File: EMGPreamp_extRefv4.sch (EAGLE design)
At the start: 33 parts

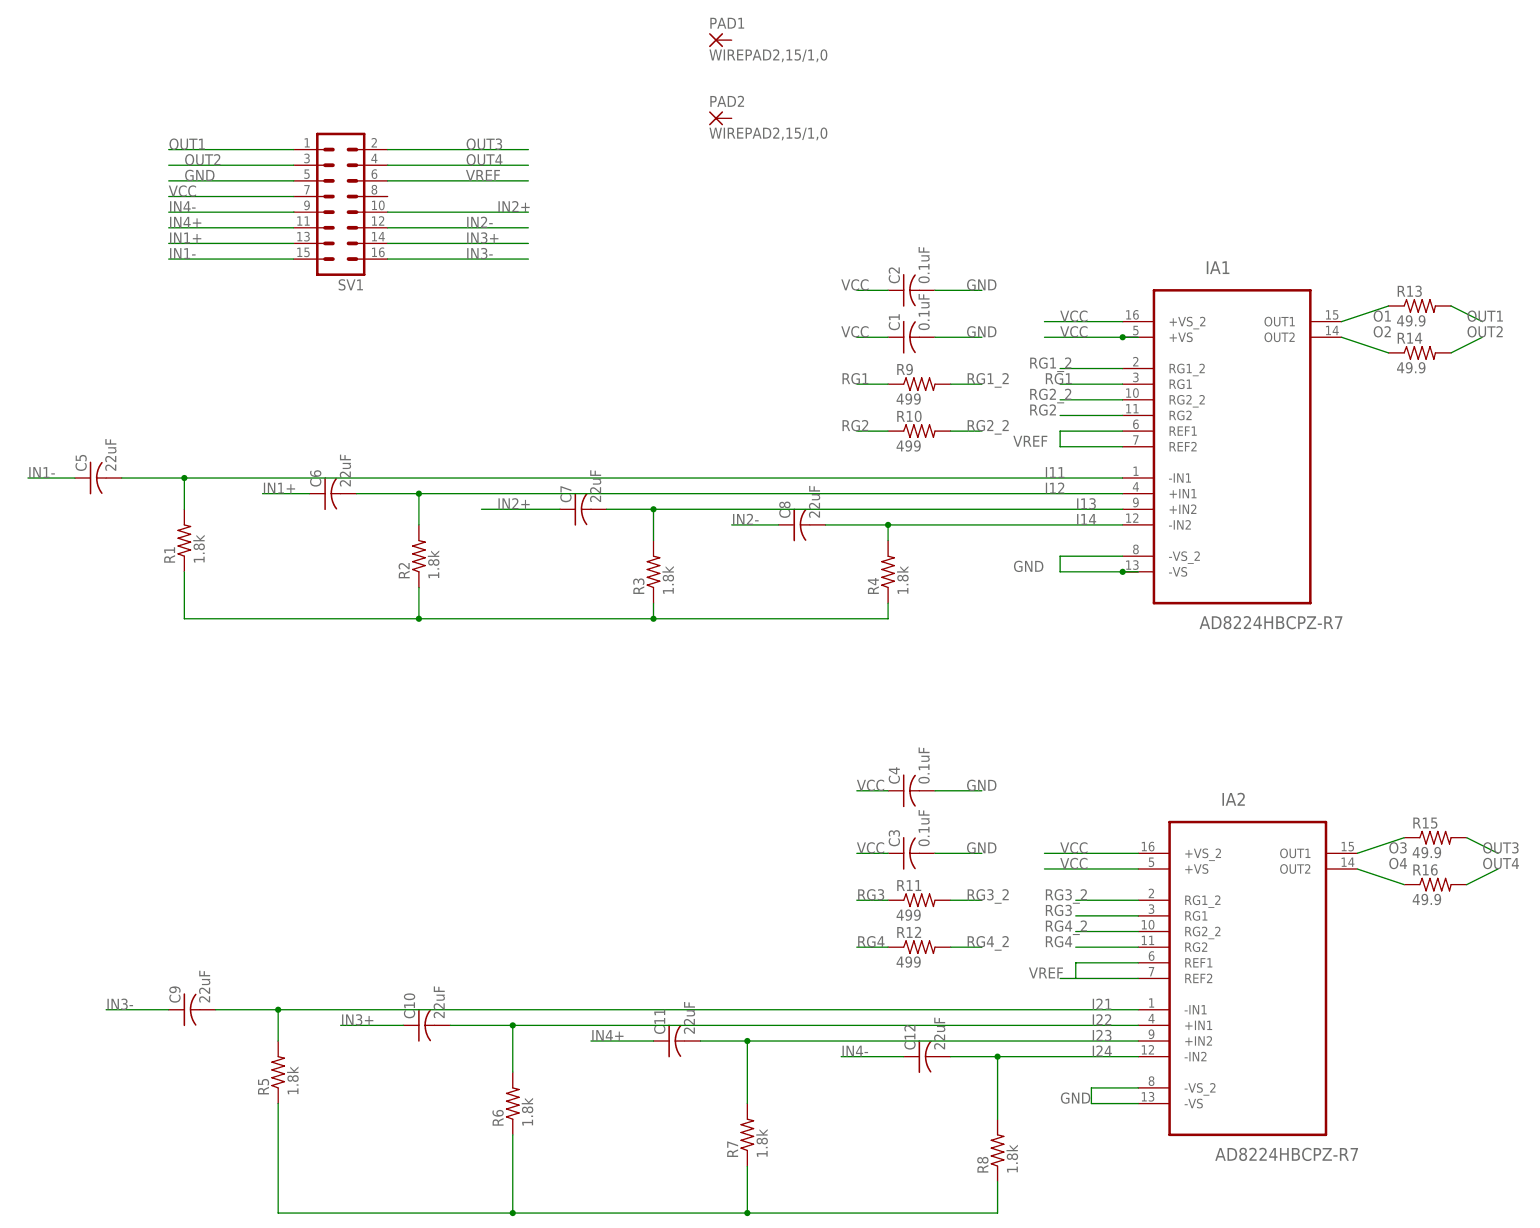
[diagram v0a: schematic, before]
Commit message: updated power board designs: v2 uses low current 2.5v reference, v3 uses 10v rail and 5v ref both with simple linear regulators. Added breakout board to go from DB37 to BNC
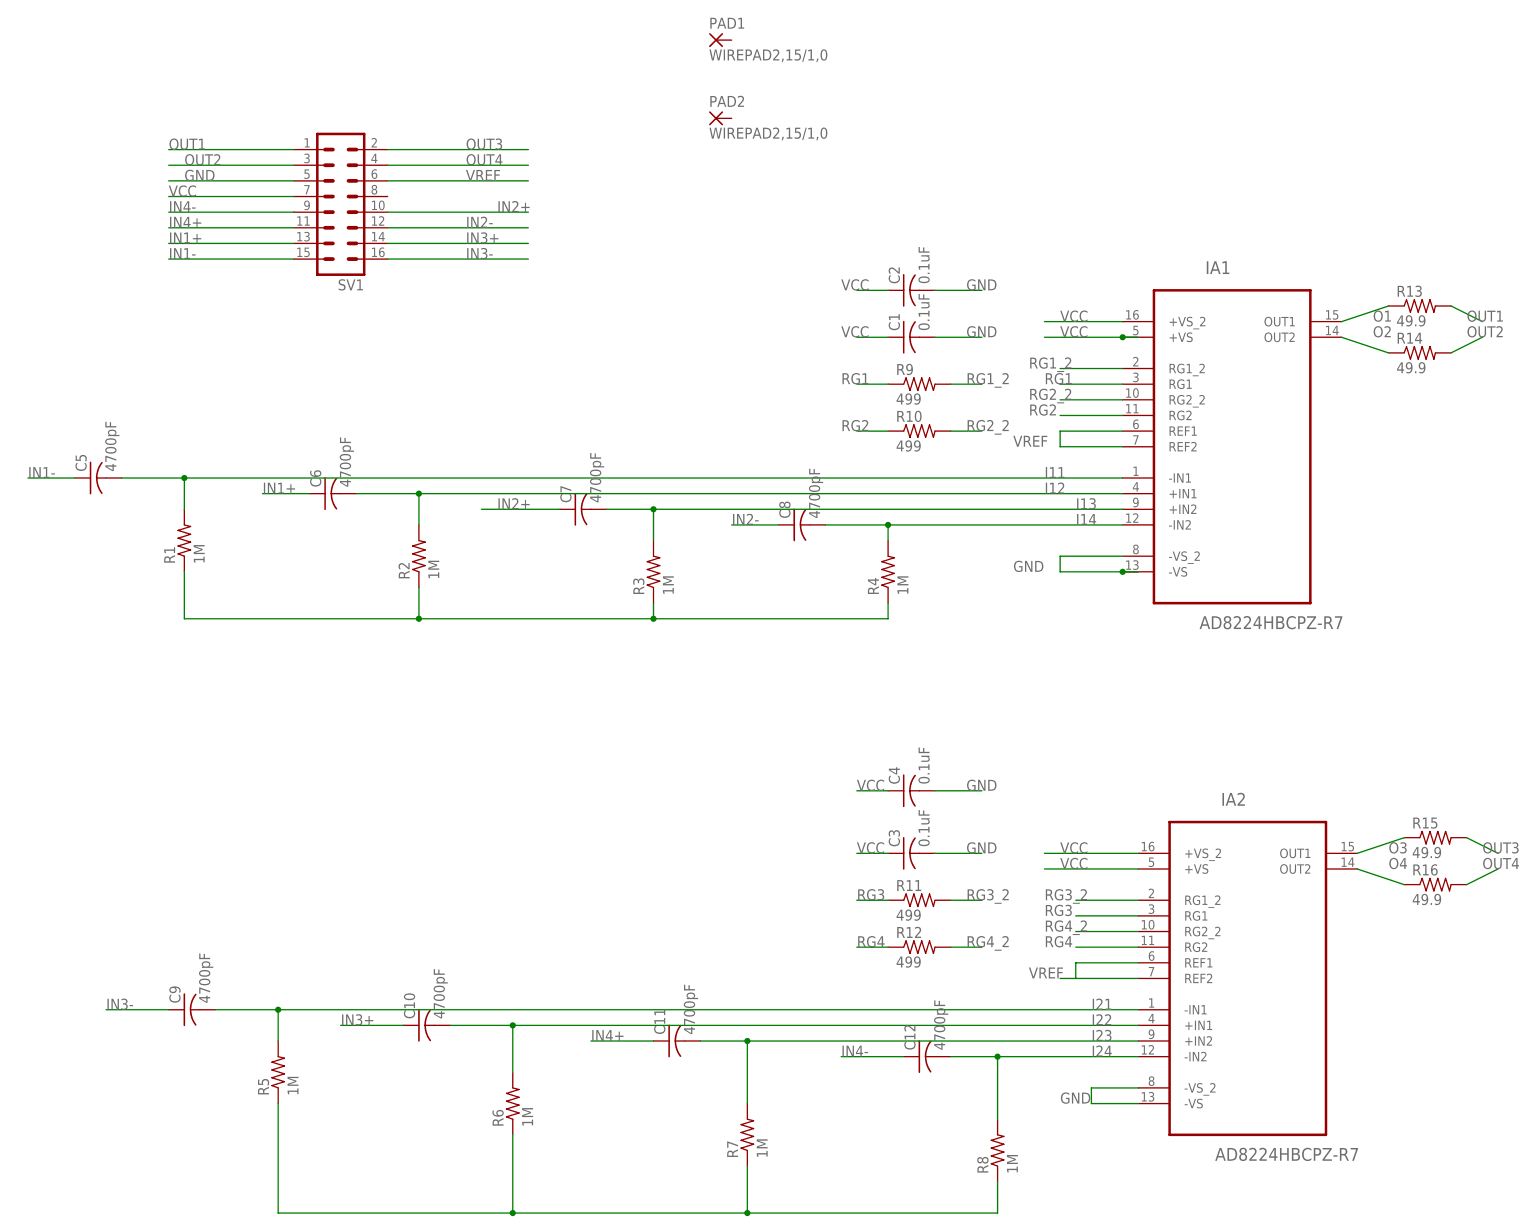
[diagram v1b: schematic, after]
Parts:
- C10, C11, C12, C5, C6, C7, C8, C9: value 22uF -> 4700pF
- R1, R2, R3, R4, R5, R6, R7, R8: value 1.8k -> 1M
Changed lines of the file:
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@@
 <part name="R11" library="rcl" deviceset="R-US_" device="R0805" value="499"/>
 <part name="R12" library="rcl" deviceset="R-US_" device="R0805" value="499"/>
-<part name="C5" library="rcl" deviceset="C-US" device="C0805" value="22uF"/>
-<part name="C6" library="rcl" deviceset="C-US" device="C0805" value="22uF"/>
-<part name="C7" library="rcl" deviceset="C-US" device="C0805" value="22uF"/>
-<part name="C8" library="rcl" deviceset="C-US" device="C0805" value="22uF"/>
-<part name="C9" library="rcl" deviceset="C-US" device="C0805" value="22uF"/>
-<part name="C10" library="rcl" deviceset="C-US" device="C0805" value="22uF"/>
-<part name="C11" library="rcl" deviceset="C-US" device="C0805" value="22uF"/>
-<part name="C12" library="rcl" deviceset="C-US" device="C0805" value="22uF"/>
+<part name="C5" library="rcl" deviceset="C-US" device="C0805" value="4700pF"/>
+<part name="C6" library="rcl" deviceset="C-US" device="C0805" value="4700pF"/>
+<part name="C7" library="rcl" deviceset="C-US" device="C0805" value="4700pF"/>
+<part name="C8" library="rcl" deviceset="C-US" device="C0805" value="4700pF"/>
+<part name="C9" library="rcl" deviceset="C-US" device="C0805" value="4700pF"/>
+<part name="C10" library="rcl" deviceset="C-US" device="C0805" value="4700pF"/>
+<part name="C11" library="rcl" deviceset="C-US" device="C0805" value="4700pF"/>
+<part name="C12" library="rcl" deviceset="C-US" device="C0805" value="4700pF"/>
 <part name="C1" library="rcl" deviceset="C-US" device="C0805" value="0.1uF"/>
 <part name="C2" library="rcl" deviceset="C-US" device="C0805" value="0.1uF"/>
@@
 <part name="PAD2" library="wirepad" deviceset="WIREPAD" device="2,15/1,0" value="WIREPAD2,15/1,0"/>
 <part name="SV1" library="con-lstb" deviceset="MA08-2W" device=""/>
-<part name="R1" library="resistor" deviceset="R-US_" device="R0805" value="1.8k"/>
-<part name="R2" library="resistor" deviceset="R-US_" device="R0805" value="1.8k"/>
-<part name="R3" library="resistor" deviceset="R-US_" device="R0805" value="1.8k"/>
-<part name="R4" library="resistor" deviceset="R-US_" device="R0805" value="1.8k"/>
-<part name="R5" library="resistor" deviceset="R-US_" device="R0805" value="1.8k"/>
-<part name="R6" library="resistor" deviceset="R-US_" device="R0805" value="1.8k"/>
-<part name="R7" library="resistor" deviceset="R-US_" device="R0805" value="1.8k"/>
-<part name="R8" library="resistor" deviceset="R-US_" device="R0805" value="1.8k"/>
+<part name="R1" library="resistor" deviceset="R-US_" device="R0805" value="1M"/>
+<part name="R2" library="resistor" deviceset="R-US_" device="R0805" value="1M"/>
+<part name="R3" library="resistor" deviceset="R-US_" device="R0805" value="1M"/>
+<part name="R4" library="resistor" deviceset="R-US_" device="R0805" value="1M"/>
+<part name="R5" library="resistor" deviceset="R-US_" device="R0805" value="1M"/>
+<part name="R6" library="resistor" deviceset="R-US_" device="R0805" value="1M"/>
+<part name="R7" library="resistor" deviceset="R-US_" device="R0805" value="1M"/>
+<part name="R8" library="resistor" deviceset="R-US_" device="R0805" value="1M"/>
 </parts>
 <sheets>

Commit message: updated design to add RF lowpass and decoupling to input. Also added real ground plane and VREF plane to help isolate inputs from noise
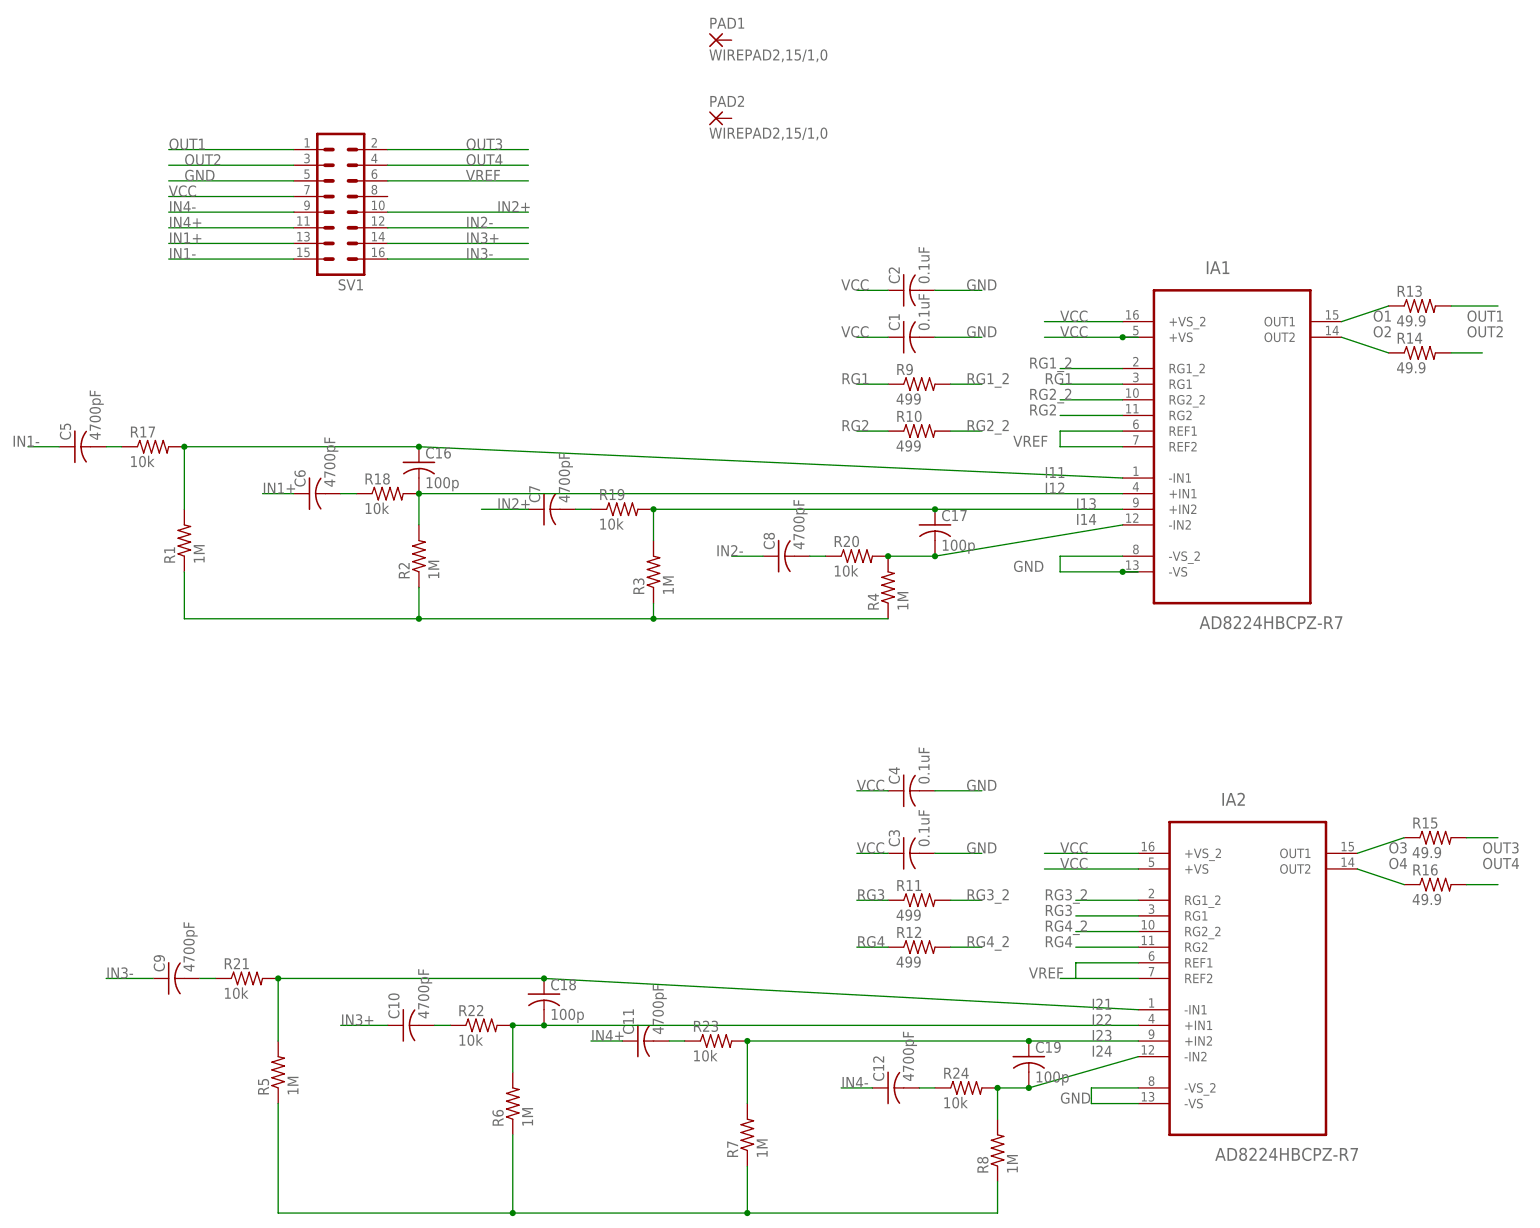
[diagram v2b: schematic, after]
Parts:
- added C16, C17, C18, C19: 100p, resistor:C-USC0805
- added R17, R18, R19, R20, R21, R22, R23, R24: 10k, resistor:R-US_R0805
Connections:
- new net N$1: C5.2, R17.1
- new net N$2: C6.2, R18.1
- new net N$3: C8.2, R20.1
- new net N$4: C9.2, R21.1
- new net N$5: C10.2, R22.1
- new net N$6: C7.2, R19.1
- new net N$7: C11.2, R23.1
- new net N$8: C12.2, R24.1
- net I11: now also C16.1, R17.2; no longer C5.2
- net I12: now also C16.2, R18.2; no longer C6.2
- net I13: now also C17.1, R19.2; no longer C7.2
- net I14: now also C17.2, R20.2; no longer C8.2
- net I21: now also C18.1, R21.2; no longer C9.2
- net I22: now also C18.2, R22.2; no longer C10.2
- net I23: now also C19.1, R23.2; no longer C11.2
- net I24: now also C19.2, R24.2; no longer C12.2
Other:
- moved on the sheet: C10, C11, C12, C5, C6, C7, C8, C9, R4
